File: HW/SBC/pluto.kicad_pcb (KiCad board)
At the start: 2 copper layers, 39 parts, among them J1 Serial Port, J2 CONN_02X07, J3 CONN_02X07, J4 POWER IN, J5 Expansion Port, Q1 DS1813, SW1 RESET, U1 WD65C02_, U10 74LS138, U11 LM7805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

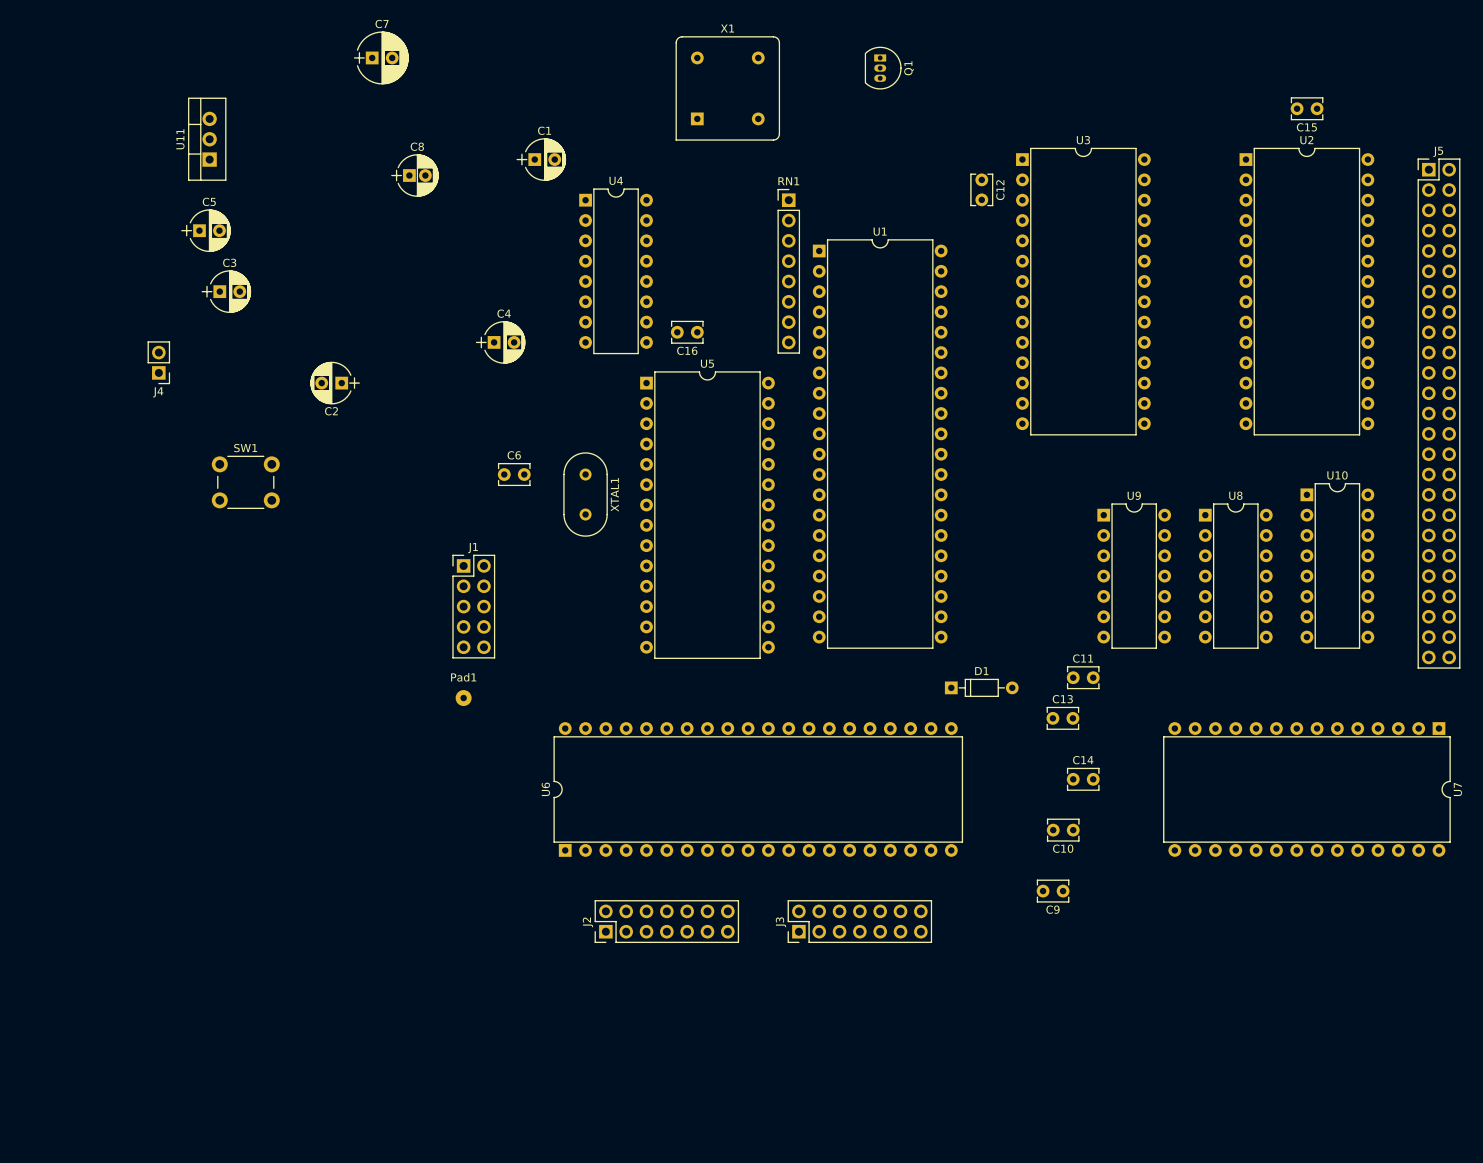
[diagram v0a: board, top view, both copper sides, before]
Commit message: New MB design. Includes RTC. New IDE design.
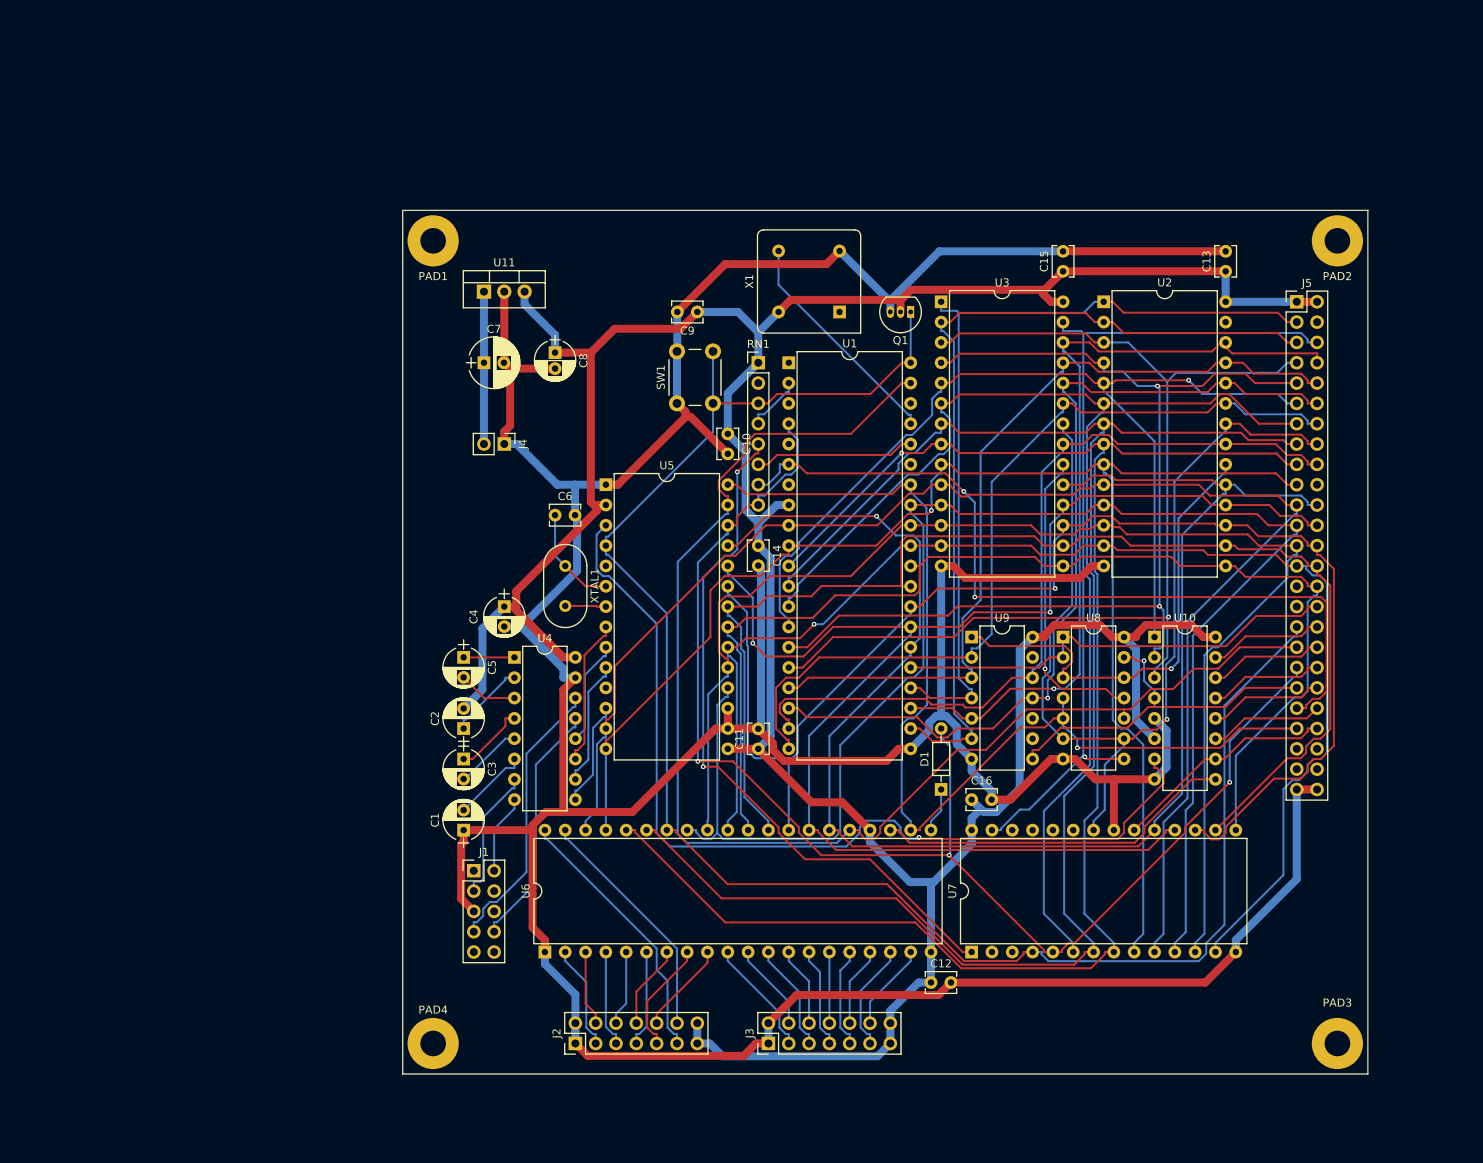
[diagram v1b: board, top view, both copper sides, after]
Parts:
- removed Pad1: RI, Wire_Pads:SolderWirePad_single_0-8mmDrill
- added PAD1: MountingHole_3.2mm_M3_Pad, Mounting_Holes:MountingHole_3.2mm_M3_Pad, F.Cu at (88.9, 40.6)
- added PAD2: MountingHole_3.2mm_M3_Pad, Mounting_Holes:MountingHole_3.2mm_M3_Pad, F.Cu at (201.9, 40.6)
- added PAD3: MountingHole_3.2mm_M3_Pad, Mounting_Holes:MountingHole_3.2mm_M3_Pad, F.Cu at (201.9, 141.0)
- added PAD4: MountingHole_3.2mm_M3_Pad, Mounting_Holes:MountingHole_3.2mm_M3_Pad, F.Cu at (88.9, 141.0)
- U11: value LM7805 -> LM7805CT
- moved C12 100.5 mm to (151.1, 133.3), turned to 0 degrees
- moved C9 85.6 mm to (121.9, 49.5)
- moved C1 84.3 mm to (92.7, 114.3), turned to 90 degrees
- moved C16 67.7 mm to (156.2, 110.5), turned to 0 degrees
- moved C3 65.9 mm to (92.7, 105.4), turned to 270 degrees
- moved C10 65.7 mm to (125.7, 64.8), turned to 270 degrees
- moved U7 64.8 mm to (156.2, 129.5), turned to 90 degrees
- moved C5 62.7 mm to (92.7, 92.7), turned to 270 degrees
- moved C13 59.9 mm to (188.0, 44.5), turned to 90 degrees
- moved U4 57.8 mm to (99.1, 92.7)
- moved SW1 57.7 mm to (119.4, 61.0), turned to 90 degrees
- moved C14 49.0 mm to (129.5, 78.7), turned to 270 degrees
- moved C2 45.8 mm to (92.7, 101.6), turned to 90 degrees
- moved J4 44.1 mm to (97.8, 66.0), turned to 270 degrees
- moved C7 40.6 mm to (95.2, 55.9)
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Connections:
- J1 pad 1: Net-(J1-Pad1) -> (no net)
- J1 pad 10: Net-(J1-Pad10) -> (no net)
- J1 pad 4: Net-(J1-Pad4) -> (no net)
- J1 pad 6: Net-(J1-Pad6) -> (no net)
- J1 pad 9: Net-(J1-Pad9) -> (no net)
- J5 pad 20: Net-(J5-Pad20) -> (no net)
- J5 pad 29: Net-(J5-Pad29) -> (no net)
- J5 pad 31: Net-(J5-Pad31) -> (no net)
- J5 pad 4: Net-(J5-Pad4) -> (no net)
- J5 pad 44: Net-(J5-Pad44) -> ~7FAX
- J5 pad 45: Net-(J5-Pad45) -> (no net)
- J5 pad 46: Net-(J5-Pad46) -> (no net)
- J5 pad 47: Net-(J5-Pad47) -> (no net)
- J5 pad 48: Net-(J5-Pad48) -> (no net)
- RN1 pad 2: Net-(RN1-Pad2) -> (no net)
- U1 pad 1: Net-(U1-Pad1) -> (no net)
- U1 pad 3: Net-(U1-Pad3) -> (no net)
- U1 pad 35: Net-(U1-Pad35) -> (no net)
- U1 pad 38: Net-(U1-Pad38) -> (no net)
- U1 pad 5: Net-(U1-Pad5) -> (no net)
- U1 pad 7: Net-(U1-Pad7) -> (no net)
- U11 pad 1: (no net) -> /Power and expansion port/+9V
- U11 pad 2: (no net) -> GND
- U11 pad 3: (no net) -> VCC
- U2 pad 27: Net-(U2-Pad27) -> (no net)
- U5 pad 11: Net-(U5-Pad11) -> (no net)
- U5 pad 5: Net-(U5-Pad5) -> (no net)
- U7 pad 23: Net-(U7-Pad23) -> (no net)
- U7 pad 24: Net-(U7-Pad24) -> (no net)
- U7 pad 26: Net-(U7-Pad26) -> (no net)
- X1 pad 1: Net-(X1-Pad1) -> (no net)
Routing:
- net GND: track 0.00 -> 544.9 mm
- net VCC: track 0.00 -> 408.6 mm
- net ~RES: track 0.00 -> 223.8 mm
- net A3: track 0.00 -> 209.6 mm
- net A2: track 0.00 -> 207.6 mm, vias 0 -> 1
- net D0: track 0.00 -> 196.1 mm
- net D7: track 0.00 -> 191.2 mm, vias 0 -> 1
- net A1: track 0.00 -> 184.9 mm, vias 0 -> 1
- net A0: track 0.00 -> 182.8 mm
- net D6: track 0.00 -> 178.3 mm, vias 0 -> 2
- net D5: track 0.00 -> 173.4 mm, vias 0 -> 1
- net ~IRQ: track 0.00 -> 171.0 mm, vias 0 -> 3
- net CLK: track 0.00 -> 168.0 mm
- net D1: track 0.00 -> 165.2 mm
- net D2: track 0.00 -> 160.1 mm, vias 0 -> 1
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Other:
- board outline added: 120.7 x 108 mm

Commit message: New board layout. WIP
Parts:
- removed C15, C16: .1uF, Capacitors_ThroughHole:C_Disc_D3.8mm_W2.6mm_P2.50mm
- removed PAD1, PAD2, PAD3, PAD4: MountingHole_3.2mm_M3_Pad, Mounting_Holes:MountingHole_3.2mm_M3_Pad
- added C17: 22pF, Capacitors_ThroughHole:C_Disc_D3.8mm_W2.6mm_P2.50mm, F.Cu at (124.5, 44.5)
- added MK1: Mounting_Hole, Mounting_Holes:MountingHole_3.2mm_M3_Pad, F.Cu at (40.6, 33.0)
- added MK2: Mounting_Hole, Mounting_Holes:MountingHole_3.2mm_M3_Pad, F.Cu at (182.9, 33.0)
- added MK3: Mounting_Hole, Mounting_Holes:MountingHole_3.2mm_M3_Pad, F.Cu at (182.9, 115.6)
- added MK4: Mounting_Hole, Mounting_Holes:MountingHole_3.2mm_M3_Pad, F.Cu at (40.6, 115.6)
- C10, C11, C12, C13, C14, C9: value .1uF -> 0.1uF
- J1: footprint Pin_Headers:Pin_Header_Straight_2x05_Pitch2.54mm -> Connect:IDC_Header_Straight_10pins
- J2, J3: footprint Pin_Headers:Pin_Header_Straight_2x07_Pitch2.54mm -> Connect:IDC_Header_Straight_14pins
- J5: footprint Pin_Headers:Pin_Header_Straight_2x25_Pitch2.54mm -> Connect:IDC_Header_Straight_50pins
- X1: footprint Oscillators:Oscillator_DIP-8 -> Housings_DIP:DIP-8_W7.62mm
- moved J5 156.3 mm to (40.6, 44.5), turned to 270 degrees
- moved U2 117.5 mm to (55.9, 36.2)
- moved U10 109.8 mm to (69.8, 78.7)
- moved U7 108.8 mm to (100.3, 36.2), turned to 0 degrees
- moved U1 97.8 mm to (55.9, 115.6), turned to 90 degrees
- moved J3 93.3 mm to (182.9, 63.5)
- moved J2 87.0 mm to (182.9, 99.1)
- moved X1 85.8 mm to (63.5, 88.9), turned to 270 degrees
- moved U8 85.6 mm to (82.5, 81.3)
- moved U6 81.9 mm to (170.8, 83.8), turned to 180 degrees
- moved J4 80.7 mm to (171.4, 99.1), turned to 0 degrees
- moved U11 76.1 mm to (128.3, 115.6), turned to 180 degrees
- moved U3 74.6 mm to (78.7, 36.2)
- moved D1 73.7 mm to (151.1, 35.6), turned to 270 degrees
- moved J1 64.9 mm to (158.8, 115.6)
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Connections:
- C10 pad 1: VCC -> Net-(C10-Pad1)
- C10 pad 2: GND -> Net-(C10-Pad2)
- C11 pad 1: VCC -> Net-(C11-Pad1)
- C11 pad 2: GND -> Net-(C11-Pad2)
- C12 pad 1: VCC -> Net-(C12-Pad1)
- C12 pad 2: GND -> Net-(C12-Pad2)
- C13 pad 1: VCC -> Net-(C13-Pad1)
- C13 pad 2: GND -> Net-(C13-Pad2)
- C14 pad 1: VCC -> Net-(C14-Pad1)
- C14 pad 2: GND -> Net-(C14-Pad2)
- C2 pad 2: VCC -> Net-(C2-Pad2)
- C4 pad 1: VCC -> Net-(C2-Pad2)
- C6 pad 1: Net-(C6-Pad1) -> GND
- C6 pad 2: GND -> Net-(C6-Pad2)
- C9 pad 1: VCC -> Net-(C9-Pad1)
- C9 pad 2: GND -> Net-(C9-Pad2)
- U1 pad 21: GND -> Net-(C9-Pad2)
- U1 pad 8: VCC -> Net-(C9-Pad1)
- U2 pad 14: GND -> Net-(C10-Pad1)
- U2 pad 27: (no net) -> Net-(C10-Pad2)
- U2 pad 28: VCC -> Net-(C10-Pad2)
- U3 pad 14: GND -> Net-(C11-Pad1)
- U3 pad 28: VCC -> Net-(C11-Pad2)
- U4 pad 16: VCC -> Net-(C2-Pad2)
- U5 pad 1: GND -> Net-(C12-Pad2)
- U5 pad 15: VCC -> Net-(C12-Pad1)
- U5 pad 6: Net-(C6-Pad1) -> Net-(C17-Pad2)
- U5 pad 7: Net-(U5-Pad7) -> Net-(C6-Pad2)
- U6 pad 1: GND -> Net-(C13-Pad2)
- U6 pad 20: VCC -> Net-(C13-Pad1)
- U7 pad 14: GND -> Net-(C14-Pad2)
- U7 pad 21: GND -> Net-(C14-Pad2)
- U7 pad 28: VCC -> Net-(C14-Pad1)
- XTAL1 pad 1: Net-(C6-Pad1) -> Net-(C17-Pad2)
- XTAL1 pad 2: Net-(U5-Pad7) -> Net-(C6-Pad2)
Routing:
- net ~7FCX: track 45.2 -> 134.5 mm, vias 0 -> 1
- net RDY: track 7.26 -> 92.4 mm
- net ~7FAX: track 28.3 -> 112.8 mm, vias 0 -> 2
- net ~RES: track 223.8 -> 281.3 mm, vias 0 -> 1
- net Net-(C13-Pad1): track 0.00 -> 55.9 mm
- net ~IRQ: track 171.0 -> 223.5 mm, vias 3 -> 0
- net D3: track 144.9 -> 197.4 mm, vias 0 -> 1
- net R/~W: track 130.7 -> 180.1 mm
- net Net-(C12-Pad2): track 0.00 -> 42.2 mm
- net Net-(C9-Pad1): track 0.00 -> 40.3 mm
- net Net-(C11-Pad2): track 0.00 -> 40.3 mm, vias 0 -> 1
- net Net-(C14-Pad1): track 0.00 -> 39.6 mm
- net GND: track 544.9 -> 505.8 mm
- net /Power and expansion port/+9V: track 19.1 -> 58.2 mm
- net ~MWR: track 107.2 -> 142.7 mm
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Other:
- board size 120.7 x 108 mm -> 149.9 x 90.2 mm
